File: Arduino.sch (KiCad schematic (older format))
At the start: 21 parts

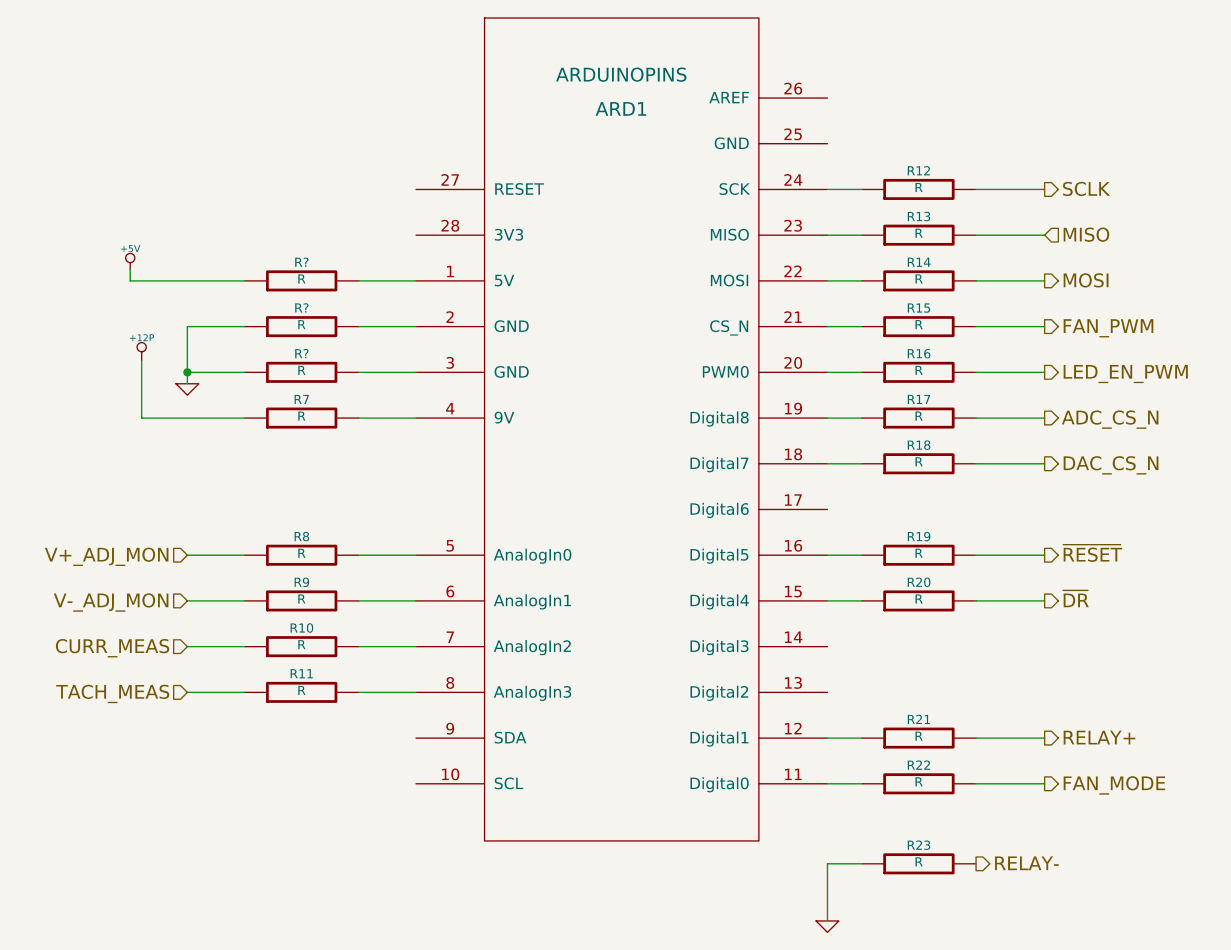
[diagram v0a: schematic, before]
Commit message: Associate and Place Power Component
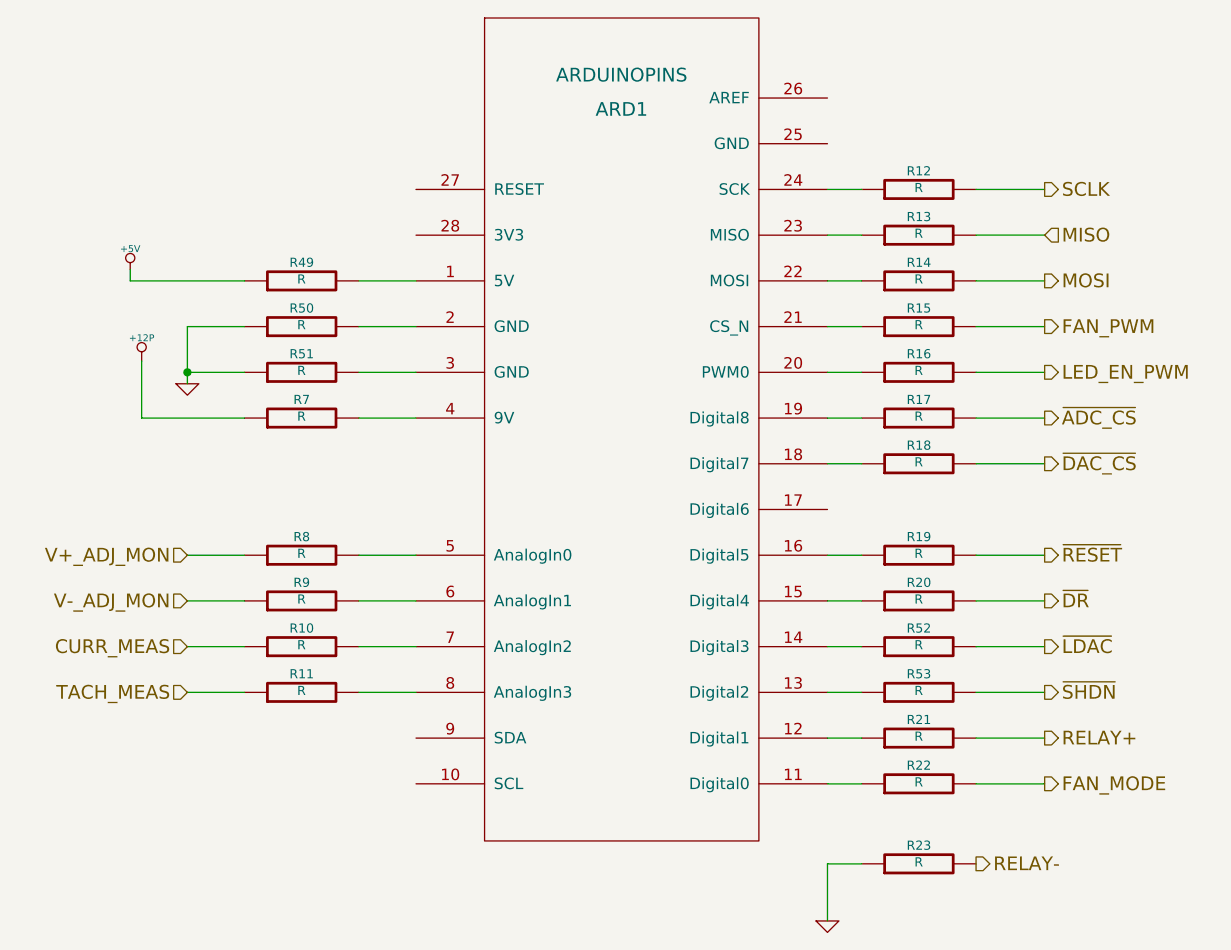
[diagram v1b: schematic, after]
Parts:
- added R52, R53: R, ~, symbol R
- gave numbers to parts that had none: 3
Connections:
- net at ARD1.13 (Digital2): now also R53.1
- net at ARD1.14 (Digital3): now also R52.1
- net ADC_CS_N renamed ~ADC_CS
- net DAC_CS_N renamed ~DAC_CS
- new net ~LDAC: R52.2
- new net ~SHDN: R53.2
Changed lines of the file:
@@
 Sheet 2 9
 Title ""
-Date "20 feb 2014"
+Date "23 feb 2014"
 Rev ""
 Comp ""
@@
 SCLK
 Text HLabel 7000 4450 2    60   Output ~ 0
-DAC_CS_N
+~DAC_CS
 Text HLabel 7000 3850 2    60   Output ~ 0
 FAN_PWM
@@
 $EndComp
 $Comp
-L GND #PWR2
+L GND #PWR01
 U 1 1 52F33146
 P 6050 6450
-F 0 "#PWR2" H 6050 6450 30  0001 C CNN
+F 0 "#PWR01" H 6050 6450 30  0001 C CNN
 F 1 "GND" H 6050 6380 30  0001 C CNN
 F 2 "" H 6050 6450 60  0000 C CNN
@@
 	6700 4050 7000 4050
 Text HLabel 7000 4250 2    60   Output ~ 0
-ADC_CS_N
+~ADC_CS
 $Comp
 L R R17
@@
 	4250 4250 4000 4250
 $Comp
-L +12P #PWR1
+L +12P #PWR02
 U 1 1 52F7B7FA
 P 3050 4000
-F 0 "#PWR1" H 3050 3970 30  0001 C CNN
+F 0 "#PWR02" H 3050 3970 30  0001 C CNN
 F 1 "+12P" H 3050 4100 30  0000 C CNN
 F 2 "" H 3050 4000 60  0000 C CNN
@@
 	6200 5050 6050 5050
 $Comp
-L R R?
+L R R51
 U 1 1 530561E5
 P 3750 4050
-F 0 "R?" V 3830 4050 40  0000 C CNN
+F 0 "R51" V 3830 4050 40  0000 C CNN
 F 1 "R" V 3757 4051 40  0000 C CNN
 F 2 "~" V 3680 4050 30  0000 C CNN
@@
 $EndComp
 $Comp
-L R R?
+L R R50
 U 1 1 530561EB
 P 3750 3850
-F 0 "R?" V 3830 3850 40  0000 C CNN
+F 0 "R50" V 3830 3850 40  0000 C CNN
 F 1 "R" V 3757 3851 40  0000 C CNN
 F 2 "~" V 3680 3850 30  0000 C CNN
@@
 $EndComp
 $Comp
-L R R?
+L R R49
 U 1 1 530561F1
 P 3750 3650
-F 0 "R?" V 3830 3650 40  0000 C CNN
+F 0 "R49" V 3830 3650 40  0000 C CNN
 F 1 "R" V 3757 3651 40  0000 C CNN
 F 2 "~" V 3680 3650 30  0000 C CNN
@@
 $EndComp
 $Comp
-L GND #PWR?
+L GND #PWR03
 U 1 1 53056214
 P 3250 4100
-F 0 "#PWR?" H 3250 4100 30  0001 C CNN
+F 0 "#PWR03" H 3250 4100 30  0001 C CNN
 F 1 "GND" H 3250 4030 30  0001 C CNN
 F 2 "" H 3250 4100 60  0000 C CNN
@@
 	4250 3650 4000 3650
 $Comp
-L +5V #PWR?
+L +5V #PWR04
 U 1 1 5305636F
 P 3000 3600
-F 0 "#PWR?" H 3000 3690 20  0001 C CNN
+F 0 "#PWR04" H 3000 3690 20  0001 C CNN
 F 1 "+5V" H 3000 3690 30  0000 C CNN
 F 2 "" H 3000 3600 60  0000 C CNN
@@
 Wire Wire Line
 	3000 3650 3000 3600
+$Comp
+L R R52
+U 1 1 530570B1
+P 6450 5250
+F 0 "R52" V 6530 5250 40  0000 C CNN
+F 1 "R" V 6457 5251 40  0000 C CNN
+F 2 "~" V 6380 5250 30  0000 C CNN
+F 3 "~" H 6450 5250 30  0000 C CNN
+	1    6450 5250
+	0    -1   -1   0
+$EndComp
+$Comp
+L R R53
+U 1 1 530570B7
+P 6450 5450
+F 0 "R53" V 6530 5450 40  0000 C CNN
+F 1 "R" V 6457 5451 40  0000 C CNN
+F 2 "~" V 6380 5450 30  0000 C CNN
+F 3 "~" H 6450 5450 30  0000 C CNN
+	1    6450 5450
+	0    -1   -1   0
+$EndComp
+Wire Wire Line
+	6050 5250 6200 5250
+Wire Wire Line
+	6200 5450 6050 5450
+Text HLabel 7000 5250 2    60   Output ~ 0
+~LDAC
+Text HLabel 7000 5450 2    60   Output ~ 0
+~SHDN
+Wire Wire Line
+	6700 5250 7000 5250
+Wire Wire Line
+	7000 5450 6700 5450
 $EndSCHEMATC
